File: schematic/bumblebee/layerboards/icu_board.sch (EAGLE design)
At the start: 1 part

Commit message: RC платок аппарата
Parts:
- added GPS: (no value), pinhead:PINHD-1X4
- added IRIDIUM: (no value), pinhead:PINHD-2X10
- added P1: B5B-EH-A, con-jst-eh:B5B-EH-A
- added R1, R2: (no value), ngspice-simulation:R
- added U$2: MCP2551, MCP2551:MCP2551
- added U$3: E22-400M22S, ebyte-radio:E22-400M22S
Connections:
- new net 3.3V: R2.2, U$1.3V3, U$3.VCC
- new net 5V_ICU: GPS.4, IRIDIUM.1, IRIDIUM.2, P1.5, U$2.VDD
- new net 7.4V: P1.4
- new net GND: GPS.1, IRIDIUM.15, IRIDIUM.18, IRIDIUM.3, IRIDIUM.4, IRIDIUM.8, P1.1, R1.2, U$2.VSS, U$3.GND
- new net N$1: IRIDIUM.5, U$1.PA4
- new net N$10: U$1.PA12, U$2.RXD
- new net N$11: R1.1, U$2.RS
- new net N$12: P1.3, U$2.CANH
- new net N$13: P1.2, U$2.CANL
- new net N$14: U$1.PB12, U$3.NSS
- new net N$15: U$1.PB13, U$3.SCK
- new net N$16: U$1.PB15, U$3.MOSI
- new net N$17: U$1.PB14, U$3.MISO
- new net N$18: R2.1, U$1.PC13, U$3.NRST
- new net N$19: U$1.PC14, U$3.BUSY
- new net N$2: GPS.3, U$1.PB10
- new net N$3: IRIDIUM.11, U$1.PA1
- new net N$4: IRIDIUM.13, U$1.PA0
- new net N$5: IRIDIUM.7, U$1.PA2
- new net N$6: IRIDIUM.6, U$1.PA3
- new net N$7: IRIDIUM.19, U$1.PA5
- new net N$8: GPS.2, U$1.PB11
- new net N$9: U$1.PA11, U$2.TXD

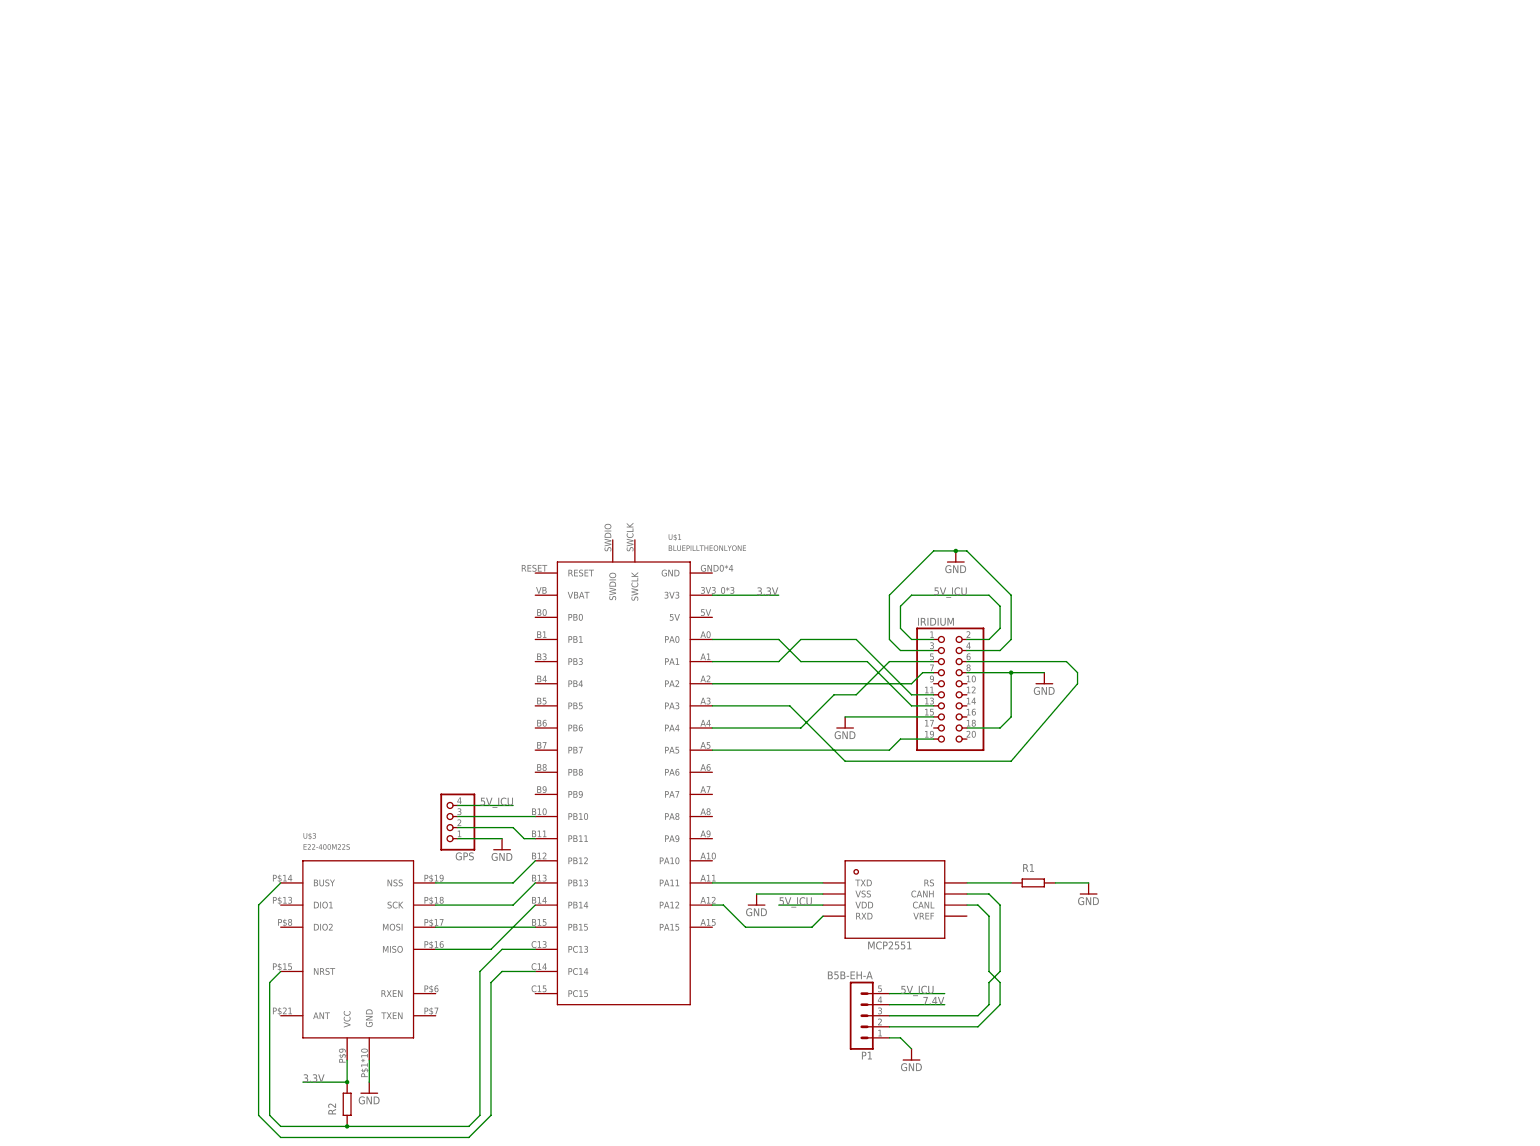
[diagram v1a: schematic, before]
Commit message: Начата работа над платами Design-block iridium ICU МК Начал переделывать схему ICU
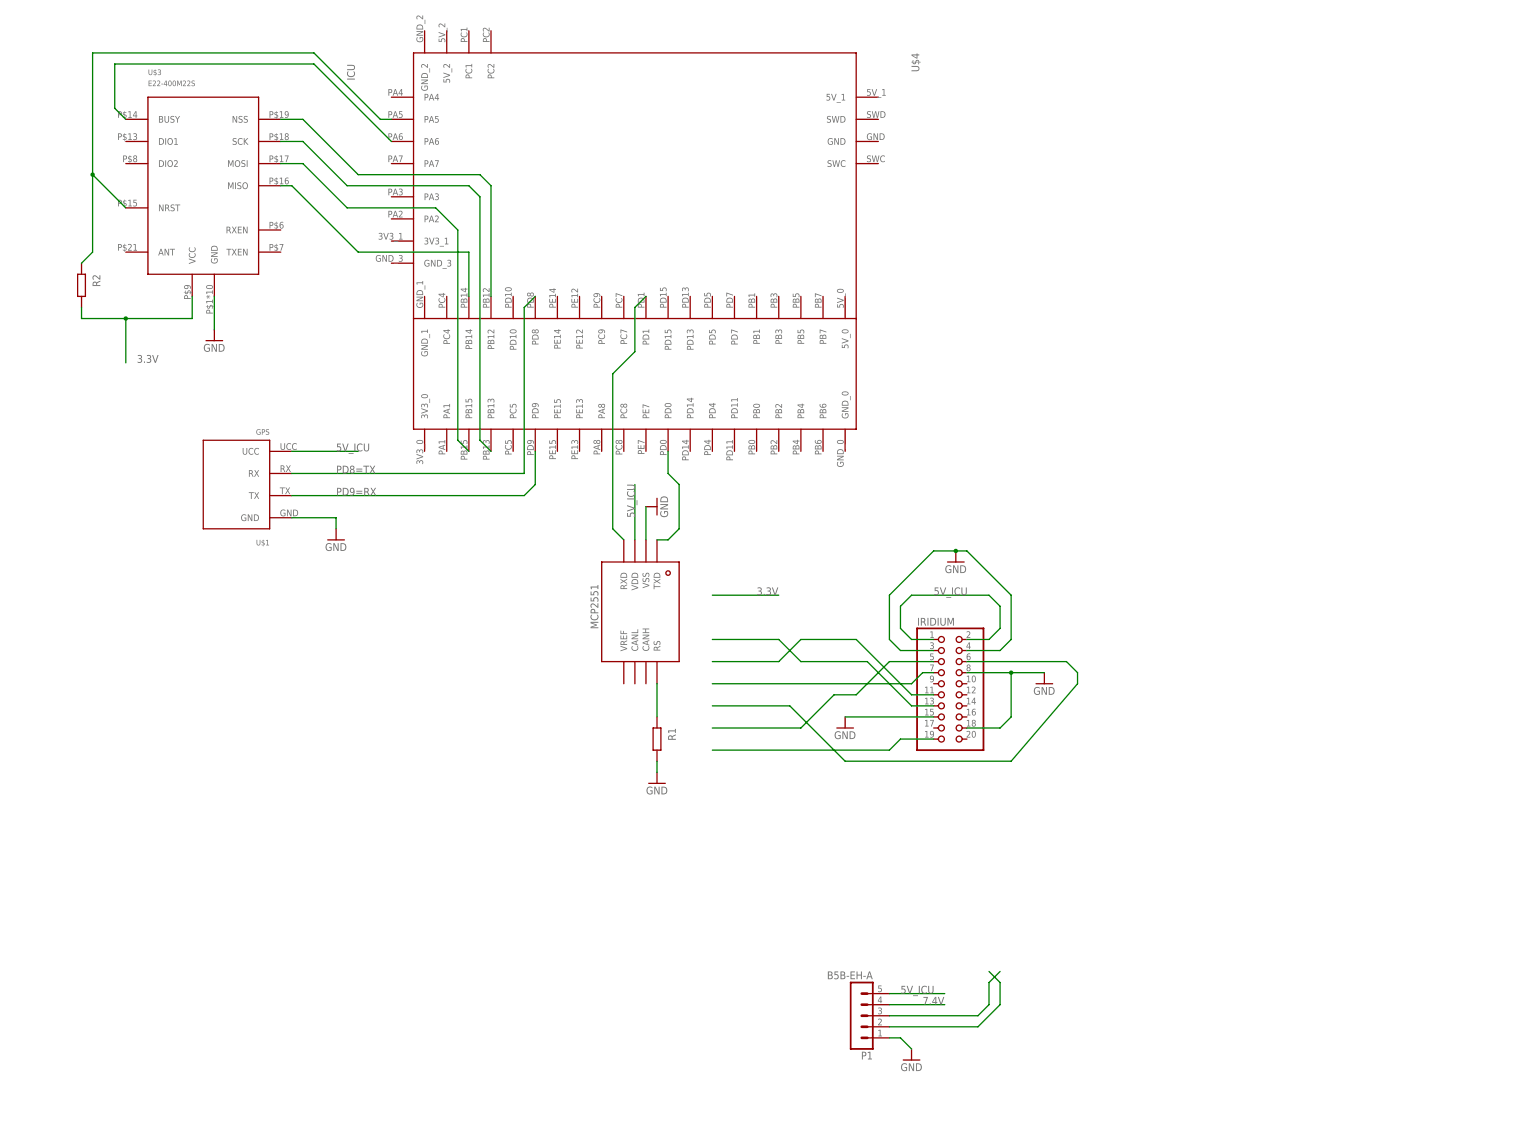
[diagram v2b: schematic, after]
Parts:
- removed GPS: (no value), pinhead:PINHD-1X4
- added U$4: ICU, bluepill:ICU
- U$1: value BLUEPILLTHEONLYONE -> GPS; device bluepill:BLUEPILLTHEONLYONE -> bluepill:GPS
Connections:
- removed net N$19: U$1.PC14, U$3.BUSY
- new net PD8=TX: U$1.RX, U$4.PD8
- new net PD9=RX: U$1.TX, U$4.PD9
- net 3.3V: no longer U$1.3V3
- net 5V_ICU: now also U$1.UCC; no longer GPS.4
- net GND: now also U$1.GND; no longer GPS.1, U$2.VSS
- net N$1: no longer U$1.PA4
- net N$10: now also U$4.PD1; no longer U$1.PA12
- net N$12: no longer U$2.CANH
- net N$13: no longer U$2.CANL
- net N$14: now also U$2.VSS; no longer U$1.PB12, U$3.NSS
- net N$15: now also U$3.MOSI, U$4.PB15; no longer U$1.PB13, U$3.SCK
- net N$16: now also U$3.MISO, U$4.PB14; no longer U$1.PB15, U$3.MOSI
- net N$17: now also U$3.BUSY, U$4.PA6; no longer U$1.PB14, U$3.MISO
- net N$18: now also U$4.PA5; no longer U$1.PC13
- net N$2: now also U$3.NSS, U$4.PB12; no longer GPS.3, U$1.PB10
- net N$3: no longer U$1.PA1
- net N$4: no longer U$1.PA0
- net N$5: no longer U$1.PA2
- net N$6: no longer U$1.PA3
- net N$7: no longer U$1.PA5
- net N$8: now also U$3.SCK, U$4.PB13; no longer GPS.2, U$1.PB11
- net N$9: now also U$4.PD0; no longer U$1.PA11
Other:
- moved on the sheet: R1, R2, U$3

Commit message: Добавлена библиотека с разьёмами для игла Design-block иридиума Вроде готовая схема ICU, но её нужно проверить и причесать
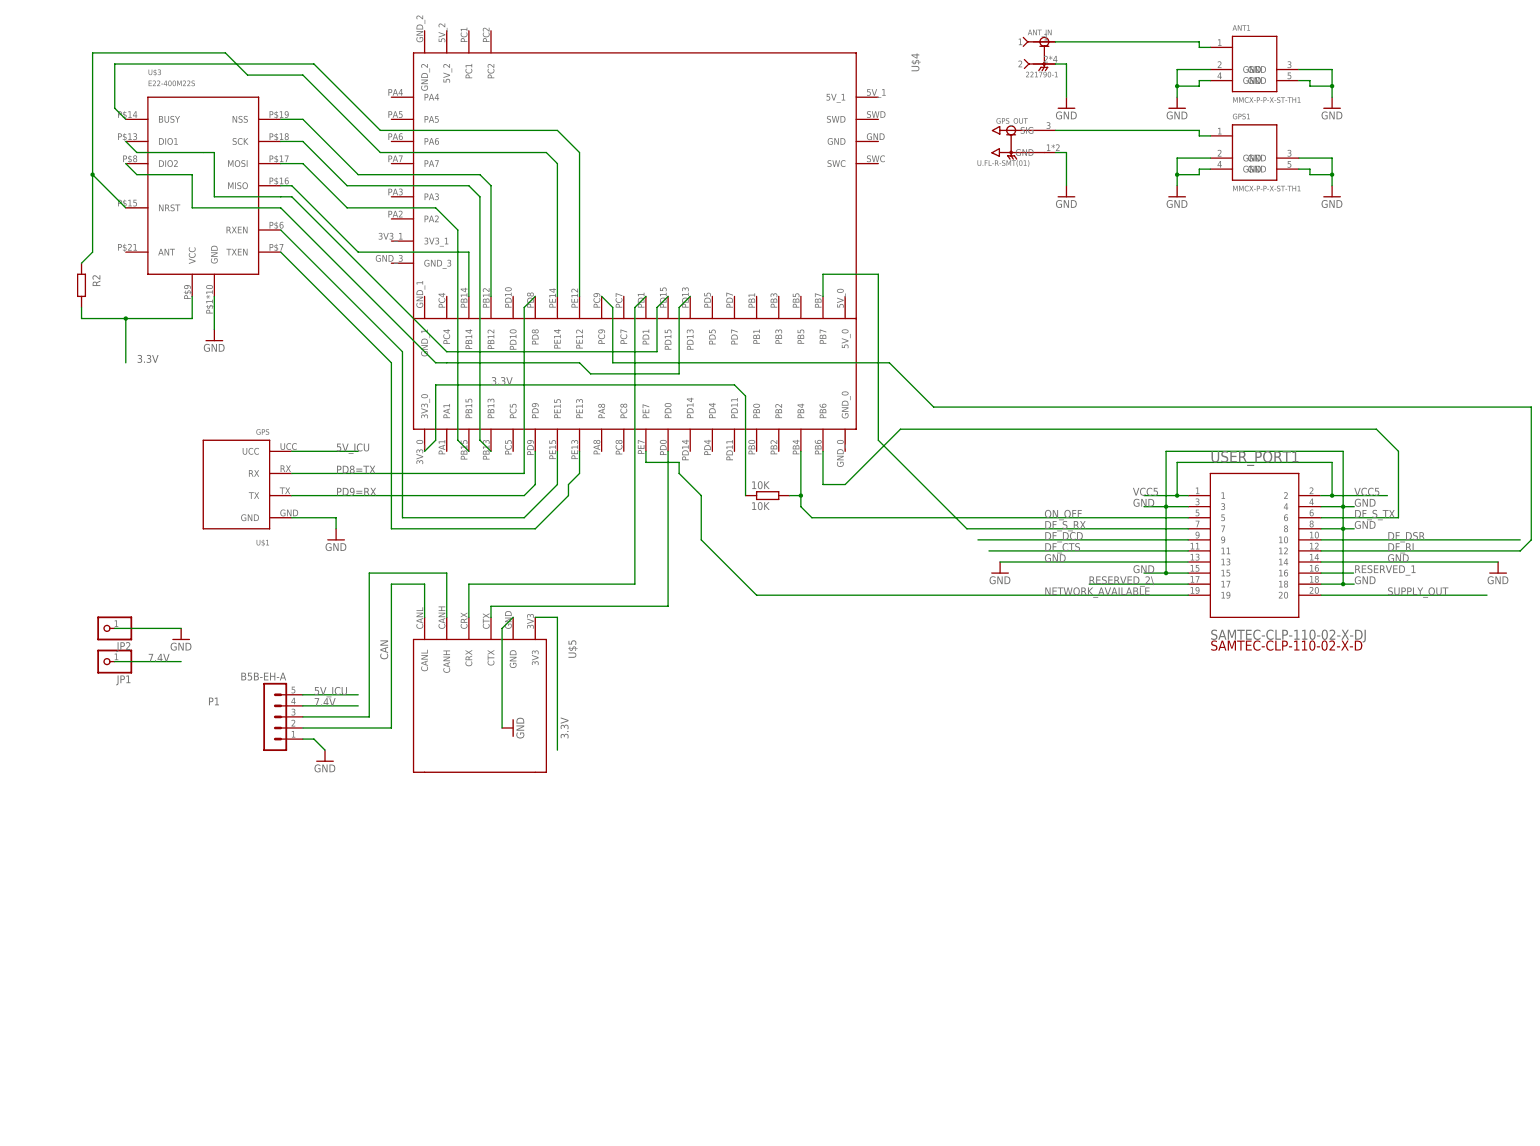
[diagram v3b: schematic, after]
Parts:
- removed IRIDIUM: (no value), pinhead:PINHD-2X10
- removed R1: (no value), ngspice-simulation:R
- removed U$2: MCP2551, MCP2551:MCP2551
- added 10K: 10K, rcl:R-EU_0204/7
- added ANT1, GPS1: MMCX-P-P-X-ST-TH1, MMCX-P-P-X-ST-TH1:MMCX-P-P-X-ST-TH1
- added ANT_IN: 221790-1, 221790-1:221790-1
- added GPS_OUT: U.FL-R-SMT(01), U.FL-R-SMT_01_:U.FL-R-SMT(01)
- added JP1, JP2: (no value), pinhead:PINHD-1X1
- added U$5: CAN, bluepill:CAN
- added USER_PORT1: SAMTEC-CLP-110-02-X-DJ, SAMTEC-CLP-110-02-X-D:SAMTEC-CLP-110-02-X-DJ
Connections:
- removed net N$11: R1.1, U$2.RS
- removed net N$14: U$2.VSS
- new net DF_CTS: USER_PORT1.11
- new net DF_DCD: USER_PORT1.9
- new net DF_DSR: USER_PORT1.10
- new net DF_RI: U$4.PC9, USER_PORT1.12
- new net DF_S_RX: U$4.PB7, USER_PORT1.7
- new net DF_S_TX: U$4.PB6, USER_PORT1.6
- new net NETWORK_AVAILABLE: U$4.PE7, USER_PORT1.19
- new net ON_OFF: 10K.2, U$4.PB4, USER_PORT1.5
- new net RESERVED_1: USER_PORT1.16
- new net RESERVED_2\: USER_PORT1.17
- new net SUPPLY_OUT: USER_PORT1.20
- new net VCC5: USER_PORT1.1, USER_PORT1.2
- net 3.3V: now also 10K.1, U$4.3V3_0, U$5.3V3
- net 5V_ICU: no longer IRIDIUM.1, IRIDIUM.2, U$2.VDD
- net 7.4V: now also JP1.1
- net GND: now also ANT1.GND@1, ANT1.GND@2, ANT1.GND@3, ANT1.GND@4, ANT_IN.2, GPS1.GND@1, GPS1.GND@2, GPS1.GND@3, GPS1.GND@4, GPS_OUT.GND, JP2.1, U$5.GND, USER_PORT1.13, USER_PORT1.14, USER_PORT1.15, USER_PORT1.18, USER_PORT1.3, USER_PORT1.4, USER_PORT1.8; no longer IRIDIUM.15, IRIDIUM.18, IRIDIUM.3, IRIDIUM.4, IRIDIUM.8, R1.2
- net N$1: now also P1.3, U$5.CANH; no longer IRIDIUM.5
- net N$10: now also U$5.CRX; no longer U$2.RXD
- net N$12: now also U$3.DIO1, U$4.PD15; no longer P1.3
- net N$13: now also U$3.DIO2, U$4.PD13; no longer P1.2
- net N$17: now also U$4.PE12; no longer U$4.PA6
- net N$18: now also U$4.PE14; no longer U$4.PA5
- net N$3: now also P1.2, U$5.CANL; no longer IRIDIUM.11
- net N$4: now also ANT1.1, ANT_IN.1; no longer IRIDIUM.13
- net N$5: now also GPS1.1, GPS_OUT.SIG; no longer IRIDIUM.7
- net N$6: now also U$3.RXEN, U$4.PE15; no longer IRIDIUM.6
- net N$7: now also U$3.TXEN, U$4.PE13; no longer IRIDIUM.19
- net N$9: now also U$5.CTX; no longer U$2.TXD
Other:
- moved on the sheet: P1

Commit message: Готовая плата ICU. Стоит посмотреть ещё раз и проверить
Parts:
- removed R2: (no value), ngspice-simulation:R
- added 10K1, 10K2: 10K, rcl:R-EU_0204/7
- added C1: (no value), rcl:CPOL-EUE3.5-8
- added C2: (no value), capacitor-wima:C2.5/2
- added GPS, IRIDIUM, MK: 332-02, con-garry:332-02
- ANT_IN: value 221790-1 -> U.FL-R-SMT(01); device 221790-1:221790-1 -> U.FL-R-SMT_01_:U.FL-R-SMT(01)
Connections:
- removed net VCC5: USER_PORT1.1, USER_PORT1.2
- new net N$11: 10K2.2, MK-2.S, U$4.PD7
- net 3.3V: now also 10K1.1, 10K2.1; no longer R2.2
- net 5V_ICU: now also C1.+, C2.2, USER_PORT1.1, USER_PORT1.2
- net DF_S_RX: now also IRIDIUM-1.S
- net DF_S_TX: now also IRIDIUM-2.S
- net GND: now also ANT_IN.GND, C1.-, C2.1, MK-1.S; no longer ANT_IN.2
- net N$18: now also 10K1.2; no longer R2.1
- net N$4: now also ANT_IN.SIG; no longer ANT_IN.1
- net PD8=TX: now also GPS-1.S
- net PD9=RX: now also GPS-2.S
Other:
- moved on the sheet: JP1, JP2, P1

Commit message: Скоро будут готовы ICU, SCU и CCU. Остались последние проверки
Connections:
- net 5V_ICU: now also U$4.5V_0
- net GND: now also U$4.GND_0, U$4.GND_1
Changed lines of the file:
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@@
 <part name="10K2" library="rcl" library_urn="urn:adsk.eagle:library:334" deviceset="R-EU_" device="0204/7" package3d_urn="urn:adsk.eagle:package:23498/1" value="10K"/>
 <part name="GND6" library="supply1" library_urn="urn:adsk.eagle:library:371" deviceset="GND" device=""/>
+<part name="GND15" library="supply1" library_urn="urn:adsk.eagle:library:371" deviceset="GND" device=""/>
+<part name="GND16" library="supply1" library_urn="urn:adsk.eagle:library:371" deviceset="GND" device=""/>
 </parts>
 <sheets>
@@
 <instance part="GND6" gate="1" x="20.32" y="152.4" smashed="yes">
 <attribute name="VALUE" x="17.78" y="149.86" size="1.778" layer="96"/>
+</instance>
+<instance part="GND15" gate="1" x="-40.64" y="111.76" smashed="yes" rot="R90">
+<attribute name="VALUE" x="-38.1" y="109.22" size="1.778" layer="96" rot="R90"/>
+</instance>
+<instance part="GND16" gate="1" x="55.88" y="81.28" smashed="yes" rot="R90">
+<attribute name="VALUE" x="58.42" y="78.74" size="1.778" layer="96" rot="R90"/>
 </instance>
 </instances>
@@
 <wire x1="-81.28" y1="-7.62" x2="-81.28" y2="-10.16" width="0.1524" layer="91"/>
 <junction x="-81.28" y="-7.62"/>
+</segment>
+<segment>
+<pinref part="U$4" gate="G$1" pin="5V_0"/>
+<wire x1="50.8" y1="106.68" x2="50.8" y2="121.92" width="0.1524" layer="91"/>
+<label x="50.8" y="114.3" size="1.778" layer="95" rot="R90"/>
 </segment>
 </net>
@@
 <wire x1="15.24" y1="157.48" x2="15.24" y2="129.54" width="0.1524" layer="91"/>
 </segment>
+<segment>
+<pinref part="U$4" gate="G$1" pin="GND_1"/>
+<wire x1="-45.72" y1="106.68" x2="-45.72" y2="111.76" width="0.1524" layer="91"/>
+<wire x1="-45.72" y1="111.76" x2="-43.18" y2="111.76" width="0.1524" layer="91"/>
+<pinref part="GND15" gate="1" pin="GND"/>
+</segment>
+<segment>
+<pinref part="U$4" gate="G$1" pin="GND_0"/>
+<wire x1="50.8" y1="71.12" x2="53.34" y2="71.12" width="0.1524" layer="91"/>
+<wire x1="53.34" y1="71.12" x2="53.34" y2="81.28" width="0.1524" layer="91"/>
+<pinref part="GND16" gate="1" pin="GND"/>
+</segment>
 </net>
